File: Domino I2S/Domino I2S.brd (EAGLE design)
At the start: 33.9 x 33 mm, 58 parts, among them J1 MH4-1, J2 MIC-45-22, J3 MH4-1, J4 MH2-1, J5 MH4-1, J6 DLT1120A, J7 MH4-1, J8 MH2-1, U1 WM8978CGEFL

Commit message: Domino I2S Rev. A: added mounting hole and silkscreen artwork
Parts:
- removed HEADPHONE1: ST-3538-050, Domino:ST-3538-050
- removed J7: MH4-1, Domino:MH4-1-0.1
- removed J8: MH2-1, Domino:MH2-1-0.1
- removed R19: 10k, Domino:R0402
- added MIC1: MIC-45-22, Domino:MIC-45-22
- added R15: 22R, Domino:R0402
- added U$12, U$14: (no value), Domino:DOMINO_LOGO_SMALL
- added U$13: (no value), Domino:CE_LOGO_SMALL
- added U$15: (no value), Domino:ESD_LOGO
- added U$16: (no value), Domino:FCC_LOGO_SMALL
- added U$17: (no value), Domino:OPEN_HARDWARE_LOGO
- added U$18: (no value), Domino:RECYCLE_BIN_LOGO
- added U$19: (no value), Domino:ROHS_LOGO
- C1: value 4u7 -> 1u
- C10: value 1n -> 220p
- C11: value 1n -> 10n
- C12: value 33p -> 1u
- C13: value 1u -> 10n
- C14: value 10n -> 1u
- C15: value 10n -> 4u7
- C16, C9: value 1u -> 4u7
- C2, C3: value 4u7 -> 33p
- C4, C5: value 4u7 -> 1n
- C7: value 220p -> 4u7
- C8: value 33p -> 4u7
- J1: value MH4-1 -> DLT1120A; device Domino:MH4-1-0.1 -> Domino:DLT1120A
- J2: value MIC-45-22 -> ST-3538-050; device Domino:MIC-45-22 -> Domino:ST-3538-050
- J3: value MH4-1 -> MH2-1; device Domino:MH4-1-0.1 -> Domino:MH2-1-0.1
- J5: value MH4-1 -> MH8-1; device Domino:MH4-1-0.1 -> Domino:MH8-1-0.1
- J6: value DLT1120A -> MH8-1; device Domino:DLT1120A -> Domino:MH8-1-0.1
- R10: value 0R -> 22R
- R11, R12: value 4k7 -> 22R
- R14: value 10k -> 22R
- R16, R17: value 0R -> 10k
- R18: value 10k -> 0R
- R2: value 0R -> 4k7
- R3: value 22R -> 4k7
- R4, R8: value 22R -> 0R
- R5: value 47k -> 0R
- R6: value 22R -> 680R
- R7: value 680R -> 47k
- R9: value 22R -> 10k
- moved J3 37.8 mm to (10.2, 31.8), turned to 0 degrees
- moved J4 30.5 mm to (10.2, 1.27), turned to 0 degrees
- moved C15 29.1 mm to (26.2, 4.64), turned to 270 degrees
- moved FB3 28.4 mm to (16.1, 29.1), flipped to the bottom, turned to 0 degrees
- moved FB4 25.8 mm to (16.3, 3.56), flipped to the top
- moved C14 22.4 mm to (19.1, 7.62), flipped to the bottom
- moved C13 22.1 mm to (15.2, 29.5), flipped to the top
- moved J2 19.4 mm to (3.43, 22.5), turned to 0 degrees
- moved C3 18.3 mm to (13.8, 17.5), flipped to the bottom, turned to 0 degrees
- moved FB6 17.5 mm to (33.1, 5.91), turned to 90 degrees
- moved J1 16.9 mm to (8.45, 10.9), turned to 90 degrees
- moved R11 16.7 mm to (22.4, 4.64), flipped to the top, turned to 90 degrees
- moved R16 16.1 mm to (29.8, 9.02), turned to 0 degrees
- moved C12 16.1 mm to (19.1, 8.76)
- moved R3 15.7 mm to (13.8, 18.7), flipped to the bottom, turned to 180 degrees
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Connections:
- net +3V3: now also C15.1, C16.1, C6.1, FB6.2, R1.1, R16.2, R4.1, R9.2; no longer C1.1, C3.1, C4.1, FB3.2, R16.1, R18.2, R19.2, R2.1
- net +5V: now also FB3.1, R5.1; no longer FB4.1, R1.1
- net ADCDAT: now also J6.3, R12.1; no longer J1.2, R6.1
- net BCLK: now also J6.7, R11.1; no longer J3.2, R4.1
- net CSB: now also R18.1; no longer R17.1
- net DACDAT: now also J6.5, R14.1; no longer J3.4, R8.1
- net GND: now also C13.2, C16.2, C3.1, C5.2, C7.1, C9.2, FB4.2, J1.1, J2.1, J2.5, R17.1, R2.2, R3.2, R7.1, R8.1; no longer C1.2, C12.1, C14.2, C3.2, C5.1, C7.2, FB6.2, HEADPHONE1.1, HEADPHONE1.5, J6.1, R10.1, R11.2, R12.2, R14.1, R5.1
- net LOUT1: now also C5.1; no longer C10.1
- net LOUT2: now also L1.1; no longer L2.1
- net LRCK: now also J6.6, R10.1; no longer J3.3, R3.1
- net MCLK: now also J6.4, R15.1; no longer J1.1, R9.1
- net MICBIAS: now also C9.1, R6.2; no longer C6.1, R7.2
- net MICN: now also C14.2, J4.1, MIC1.-, R8.2; no longer C13.2, J2.-, J8.2, R10.2
- net MICP: now also C10.1, C12.2, J4.2, MIC1.+, R6.1, R7.2; no longer C7.1, C9.2, J2.+, J8.1, R5.2, R7.1
- net MODE: now also R16.1, R17.2; no longer R13.1, R14.2
- net N$1: now also R10.2; no longer R3.2
- net N$10: now also FB4.1, J6.1; no longer FB6.1, J1.4
- net N$11: now also FB3.2, J5.1; no longer FB4.2, J5.4
- net N$12: now also R3.1; no longer R11.1
- net N$13: now also R2.1; no longer R12.1
- net N$14: now also FB6.1, J6.8; no longer FB3.1, J3.1
- net N$15: now also J5.6; no longer J7.3
- net N$16: now also C3.2, J2.3, J2.4; no longer C8.2, HEADPHONE1.3, HEADPHONE1.4
- net N$17: now also C2.2, J2.2; no longer C12.2, HEADPHONE1.2
- net N$2: now also R11.2; no longer R4.2
- net N$3: now also R12.2; no longer R6.2
- net N$4: now also R14.2; no longer R8.2
- net N$5: now also R15.2; no longer R9.2
- net N$6: now also C12.1; no longer C9.1
- net N$7: now also C14.1; no longer C13.1
- net N$8: now also C1.1, J1.3; no longer C16.1, J6.3
- net N$9: now also J1.2, R1.2; no longer J6.2, R16.2
- net ROUT1: now also C4.1; no longer C11.1
- net ROUT2: now also L2.1; no longer L1.1
- net SCLK: now also J5.4, R13.1; no longer J5.1, R18.1
- net SDIN: now also J5.5, R9.1; no longer J7.4, R19.1
- net SPDIF_OUT: now also C1.2, J6.2, R18.2; no longer C16.2, J1.3, R17.2
- net SPKL: now also C11.1, J3.1, L1.2; no longer C15.1, J4.2, L2.2
- net SPKR: now also C13.1, J3.2, L2.2; no longer C14.1, J4.1, L1.2
- net SPKVDD: now also C7.2, R4.2, R5.2; no longer C2.2, R1.2, R2.2
- net VMID: now also C8.2; no longer C5.2
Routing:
- net +5V: track 19.9 -> 26.7 mm
- net N$11: track 5.28 -> 2.67 mm
- net SDIN: track 34.3 -> 36.6 mm, vias 1 -> 2
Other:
- board size 33.9 x 33 mm -> 34.3 x 33 mm
- board text added: "+3V3"
- board text added: "+5V"
- board text added: ">DATE"
- board text added: "GDN"
- board text added: "GND"
- board text added: "I2S_CK"
- board text added: "I2S_MCK"
- board text added: "I2S_MICIN"
- board text added: "I2S_SD"
- board text added: "I2S_WS"
- board text added: "MICN"
- board text added: "MICP"
- board text added: "SCLK"
- board text added: "SDIN"
- board text added: "SPDIF OUT"
- board text added: "SPDIF_OUT"
- board text added: "SPKL"
- board text added: "SPKR"

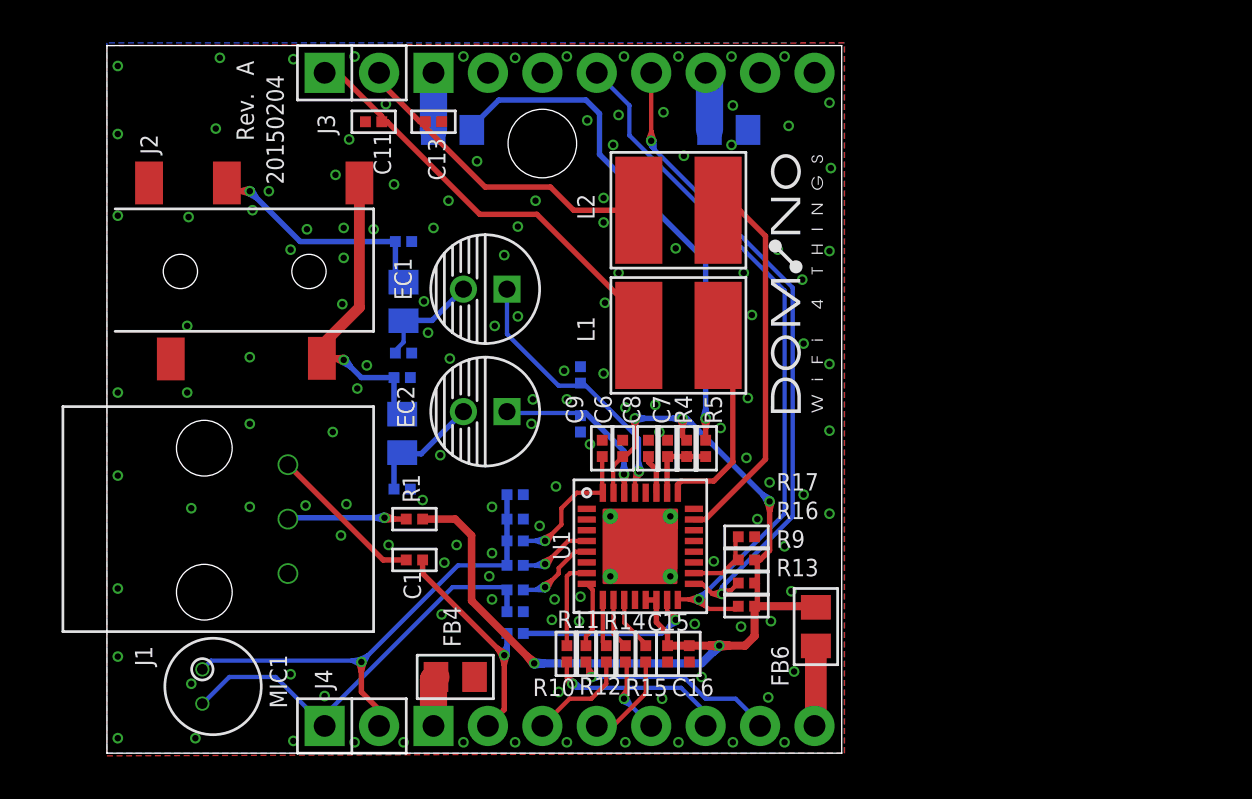
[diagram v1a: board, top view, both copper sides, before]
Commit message: Domino I2S Rev. A: started again from correct PADS files
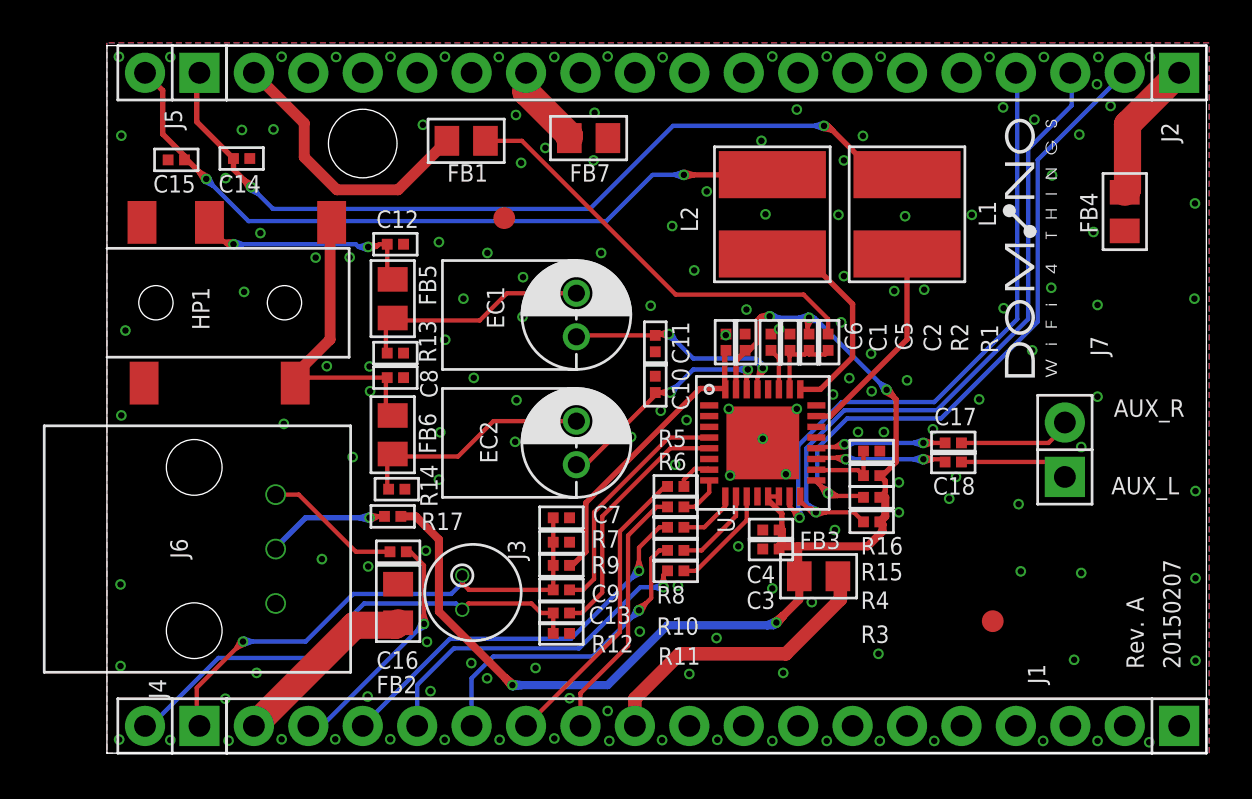
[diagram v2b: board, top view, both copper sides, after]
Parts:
- removed MIC1: MIC-45-22, Domino:MIC-45-22
- removed R18: 0R, Domino:R0402
- removed U$14: (no value), Domino:DOMINO_LOGO_SMALL
- removed U$16: (no value), Domino:FCC_LOGO_SMALL
- removed U$17: (no value), Domino:OPEN_HARDWARE_LOGO
- removed U$18: (no value), Domino:RECYCLE_BIN_LOGO
- removed U$19: (no value), Domino:ROHS_LOGO
- added C17, C18: 1u, Domino:C0402
- added F1, F2: FIDUCIAL, Domino:FIDUCIAL
- added FB7: HH-1T1005-121, Domino:FB0805
- added HP1: ST-3538-050, Domino:ST-3538-050
- added J7: MH2-1, Domino:MH2-1-0.1
- added U$20: (no value), Domino:CE_LOGO_SMALL
- added U$21: (no value), Domino:FCC_LOGO_SMALL
- added U$22: (no value), Domino:ROHS_LOGO
- C1: value 1u -> 4u7
- C10: value 220p -> 1n
- C11: value 10n -> 1n
- C12: value 1u -> 33p
- C13: value 10n -> 1u
- C14: value 1u -> 10n
- C15: value 4u7 -> 10n
- C16, C9: value 4u7 -> 1u
- C2, C3: value 33p -> 4u7
- C4, C5: value 1n -> 4u7
- C7: value 4u7 -> 220p
- C8: value 4u7 -> 33p
- EC1, EC2: value 100u -> 220u
- J1: value DLT1120A -> MH18-1; device Domino:DLT1120A -> Domino:MH18-1-0.1
- J2: value ST-3538-050 -> MH18-1; device Domino:ST-3538-050 -> Domino:MH18-1-0.1
- J3: value MH2-1 -> MIC-45-22; device Domino:MH2-1-0.1 -> Domino:MIC-45-22
- J5: value MH8-1 -> MH2-1; device Domino:MH8-1-0.1 -> Domino:MH2-1-0.1
- J6: value MH8-1 -> DLT1120A; device Domino:MH8-1-0.1 -> Domino:DLT1120A
- R12: value 22R -> 0R
- R13: value 10k -> 4k7
- R14: value 22R -> 4k7
- R15: value 22R -> 10k
- R17: value 10k -> 0R
- R2: value 4k7 -> 0R
- R3: value 4k7 -> 10k
- R4: value 0R -> 10k
- R5, R8: value 0R -> 22R
- R6: value 680R -> 22R
- R9: value 10k -> 680R
- U$13: device Domino:CE_LOGO_SMALL -> Domino:RECYCLE_BIN_LOGO
- moved J2 47.5 mm to (50.0, 31.8), turned to 180 degrees
- moved J1 42.7 mm to (50.0, 1.27), turned to 180 degrees
- moved FB4 38.0 mm to (47.5, 25.3), turned to 90 degrees
- moved C15 32.5 mm to (3.24, 27.7), turned to 180 degrees
- moved FB3 26.9 mm to (33.2, 8.26), flipped to the top, turned to 180 degrees
- moved J3 25.2 mm to (17.1, 7.49), turned to 90 degrees
- moved C14 23.8 mm to (6.29, 27.7), flipped to the top
- moved C13 23.7 mm to (21.2, 6.54), turned to 180 degrees
- moved R3 23.2 mm to (35.7, 10.8), flipped to the top, turned to 0 degrees
- moved FB6 21.7 mm to (13.3, 14.9), turned to 270 degrees
- moved R1 21.0 mm to (33.7, 19.2), turned to 270 degrees
- moved R13 20.2 mm to (13.5, 18.7)
- moved R2 20.2 mm to (32.8, 19.2), flipped to the top, turned to 270 degrees
- moved C3 19.0 mm to (31.0, 9.53), flipped to the top, turned to 180 degrees
- moved U$15 18.7 mm to (43.4, 22.0), turned to 180 degrees
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- renumbered CC-BY-SA1 to CC-BY-SA101, S1 to S101
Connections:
- new net AUXL: C18.2, U1.19
- new net AUXR: C17.2, U1.20
- new net N$18: FB4.2, J2.1
- new net N$19: C17.1, J7.2
- new net N$20: C18.1, J7.1
- net +3V3: now also C1.1, C3.1, C4.1, FB3.2, R15.2, R17.1, R2.1, R3.2, R4.2; no longer C15.1, C16.1, C6.1, FB6.2, R1.1, R13.2, R16.2, R4.1, R9.2
- net +5V: now also FB1.1, R1.1; no longer FB3.1, R5.1
- net ADCDAT: now also J1.16, R8.1; no longer J6.3, R12.1
- net BCLK: now also J1.12, R6.1; no longer J6.7, R11.1
- net CSB: now also J2.4; no longer R18.1
- net DACDAT: now also J1.14, R10.1; no longer J6.5, R14.1
- net GND: now also C1.2, C12.1, C14.2, C3.2, C5.1, C7.2, FB2.2, FB4.1, FB7.1, HP1.1, HP1.5, J6.1, R12.1, R13.2, R14.2, R16.1, U1.PAD; no longer C13.2, C16.2, C3.1, C5.2, C7.1, C9.2, FB4.2, FB5.1, J1.1, J2.1, J2.5, R17.1, R2.2, R3.2, R8.1, U1.PAD1, U1.PAD2, U1.PAD3, U1.PAD4
- net LOUT1: now also C10.1; no longer C5.1
- net LOUT2: now also L2.1; no longer L1.1
- net LRCK: now also J1.13, R5.1; no longer J6.6, R10.1
- net MCLK: now also J1.15, R11.1; no longer J6.4, R15.1
- net MICBIAS: now also C6.1, R9.2; no longer C9.1, R6.2
- net MICN: now also C13.2, J3.-, J4.2, R12.2; no longer C14.2, J4.1, MIC1.-, R8.2
- net MICP: now also C7.1, C9.2, J3.+, J4.1, R9.1; no longer C10.1, C12.2, J4.2, MIC1.+, R6.1
- net MODE: now also R15.1, R16.2; no longer R16.1, R17.2
- net N$1: now also R5.2; no longer R10.2
- net N$10: now also FB2.1, J1.18; no longer FB4.1, J6.1
- net N$11: now also FB1.2, J2.18; no longer FB3.2, J5.1
- net N$12: now also FB5.2, R13.1; no longer FB1.2, R3.1
- net N$13: now also FB6.2, R14.1; no longer FB2.2, R2.1
- net N$14: now also FB3.1, J1.11; no longer FB6.1, J6.8
- net N$15: now also FB7.2, J2.13; no longer FB5.2, J5.6
- net N$16: now also C8.2, FB6.1, HP1.3, HP1.4; no longer C3.2, FB2.1, J2.3, J2.4
- net N$17: now also C12.2, FB5.1, HP1.2; no longer C2.2, FB1.1, J2.2
- net N$2: now also R6.2; no longer R11.2
- net N$3: now also R8.2; no longer R12.2
- net N$4: now also R10.2; no longer R14.2
- net N$5: now also R11.2; no longer R15.2
- net N$6: now also C9.1; no longer C12.1
- net N$7: now also C13.1; no longer C14.1
- net N$8: now also C16.1, J6.3; no longer C1.1, J1.3
- net N$9: now also J6.2, R17.2; no longer J1.2, R1.2
- net ROUT1: now also C11.1; no longer C4.1
- net ROUT2: now also L1.1; no longer L2.1
- net SCLK: now also J2.3, R3.1; no longer J5.4, R13.1
- net SDIN: now also J2.2, R4.1; no longer J5.5, R9.1
- net SPDIF_OUT: now also C16.2, J1.17; no longer C1.2, J6.2, R18.2
- net SPKL: now also C15.1, J5.2, L2.2; no longer C11.1, J3.1, L1.2
- net SPKR: now also C14.1, J5.1, L1.2; no longer C13.1, J3.2, L2.2
- net SPKVDD: now also C2.2, R1.2, R2.2; no longer C7.2, R4.2, R5.2
- net VMID: now also C5.2; no longer C8.2
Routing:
- net SPKR: track 15.1 -> 44.5 mm, vias 0 -> 2
- net CSB: track 10.8 -> 31.1 mm
- net SPKL: track 20.4 -> 38.9 mm, vias 0 -> 2
- net ADCDAT: track 4.82 -> 21.0 mm, vias 0 -> 1
- net MCLK: track 4.38 -> 18.4 mm, vias 0 -> 1
- net DACDAT: track 5.88 -> 17.2 mm
- net AUXR: track 0.00 -> 10.7 mm, vias 0 -> 2
- net AUXL: track 0.00 -> 10.7 mm, vias 0 -> 2
- net N$11: track 2.67 -> 13.2 mm
- net N$14: track 3.76 -> 13.9 mm
- net ROUT2: track 17.6 -> 9.70 mm
- net +3V3: track 61.6 -> 68.6 mm
- net N$18: track 0.00 -> 6.63 mm
- net +5V: track 26.7 -> 20.1 mm, vias 1 -> 0
- net N$10: track 2.33 -> 8.73 mm
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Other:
- board size 34.3 x 33 mm -> 51.3 x 33 mm
- board text added: "3V3"
- board text added: "ADCDAT"
- board text added: "AUX_L"
- board text added: "AUX_R"
- board text added: "CK"
- board text added: "MCK"
- board text added: "MIC+"
- board text added: "MIC-"
- board text added: "SCK"
- board text added: "SD"
- board text added: "SPK+"
- board text added: "SPK-"
- board text added: "WS"
- board text added: "c 2014-105, Domino Team All rights reserved"
- board text removed: "GDN"
- board text removed: "SPDIF OUT"

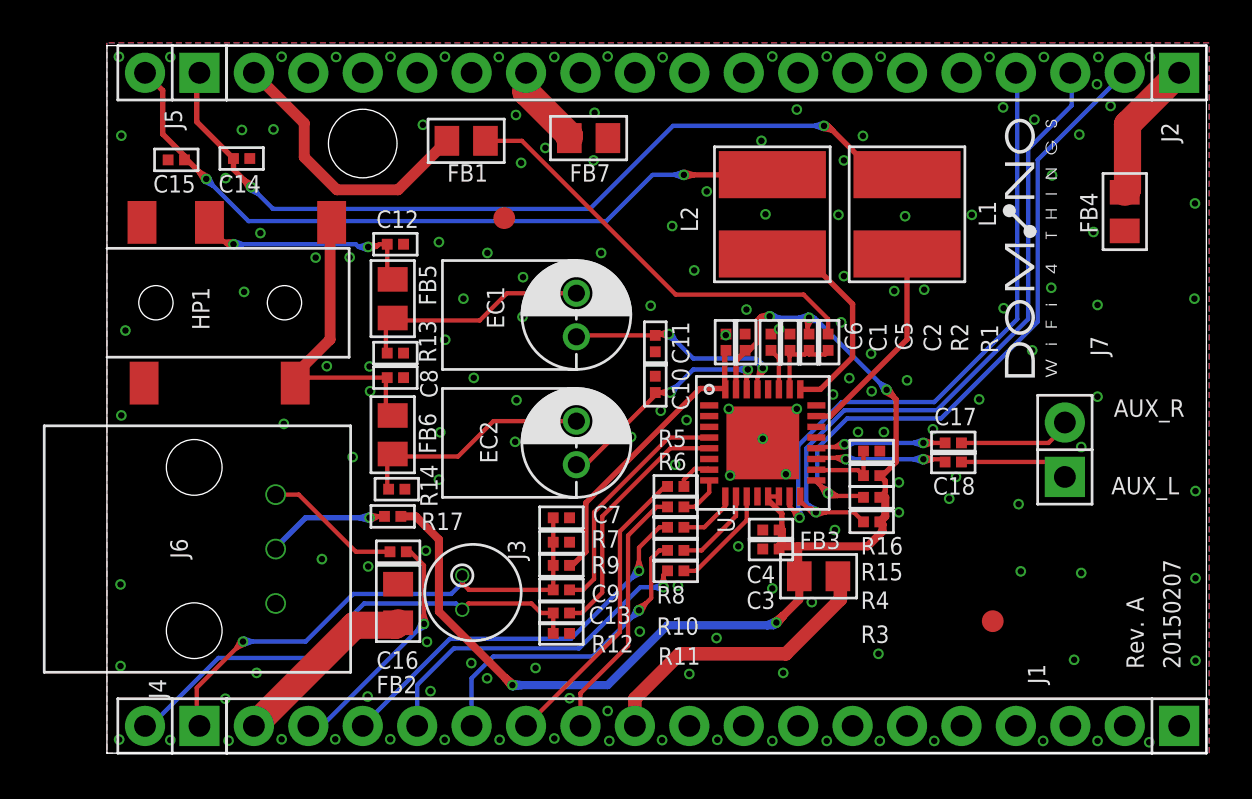
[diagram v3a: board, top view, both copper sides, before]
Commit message: Domino I2S tile Rev. B: made board multiple of 100 mils Cleaned up silkscreen made +5V trace wider Aligned some components
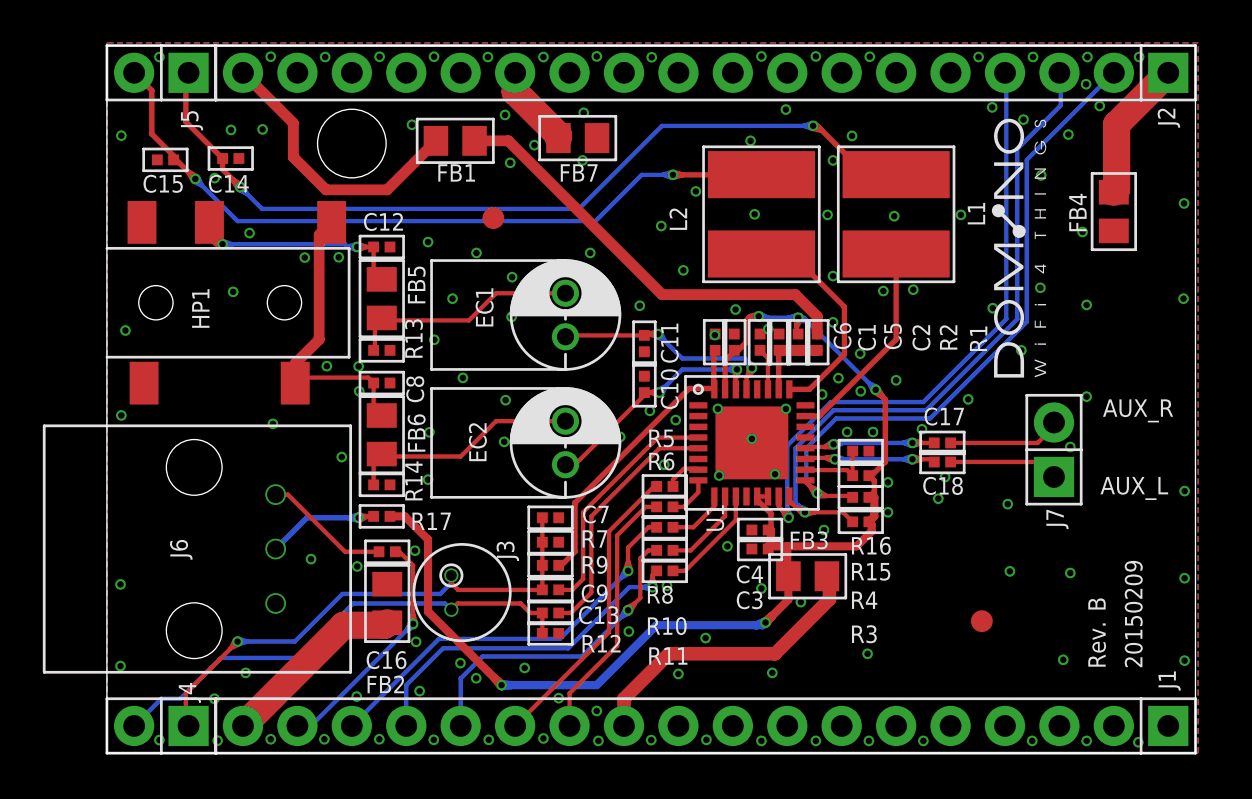
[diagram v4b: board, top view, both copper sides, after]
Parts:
- added U$14: (no value), Domino:DOMINO_LOGO_SMALL
- added U$16: (no value), Domino:OPEN_HARDWARE_LOGO
- moved U$20 32.0 mm to (41.9, 15.2), turned to 0 degrees
- moved U$22 24.7 mm to (48.3, 21.6), turned to 0 degrees
- moved U$21 23.4 mm to (33.0, 15.2), turned to 0 degrees
- moved U$15 23.1 mm to (20.3, 21.6), turned to 0 degrees
- moved U$13 19.4 mm to (27.9, 21.6), turned to 0 degrees
- moved R14 0.73 mm to (12.8, 12.5)
- moved C8 0.68 mm to (12.8, 17.3)
- moved C12 0.65 mm to (12.8, 23.6)
- moved R13 0.65 mm to (12.8, 18.8)
- moved C1 0.51 mm to (29.3, 19.2)
- moved C17 0.51 mm to (39.0, 14.5)
- moved C18 0.51 mm to (39.0, 13.6)
- moved F1 0.51 mm to (40.8, 6.16)
- moved F2 0.51 mm to (18.0, 25.0)
- moved FB3 0.51 mm to (32.7, 8.26)
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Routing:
- net N$16: track 14.6 -> 13.7 mm
- net N$9: track 8.01 -> 7.46 mm
- net N$8: track 6.62 -> 6.11 mm
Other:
- board size 51.3 x 33 mm -> 50.8 x 33 mm
